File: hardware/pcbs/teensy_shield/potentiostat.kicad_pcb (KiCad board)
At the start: 2 copper layers, 144.8 x 88.9 mm, 99 parts, among them K1 CONN_3, P1 CONN_2, P10 CONN_2, P11 CONN_2, P12 CONN_2, P13 CONN_5X2, P14 CONN_5X2, P15 CONN_2X2, P16 CONN_2X2, P17 CONN_2, P18 CONN_2, P19 CONN_2, P2 CONN_2, P20 CONN_2, P21 CONN_2, P3 CONN_2, P4 CONN_2, P5 CONN_2, P6 CONN_2, P7 CONN_2, P8 CONN_2, P9 CONN_2, U1 ZXRE060, U10 OPA227, U11 OP07, U12 LT1995, U13 ADG44X, U2 TEENSY3.1, U3 MAX6176AASA+, U4 LT1995, U5 AD8250, U6 MEA1D05XXSC, U7 OPA129, U8 OPA129, U9 ADG44X

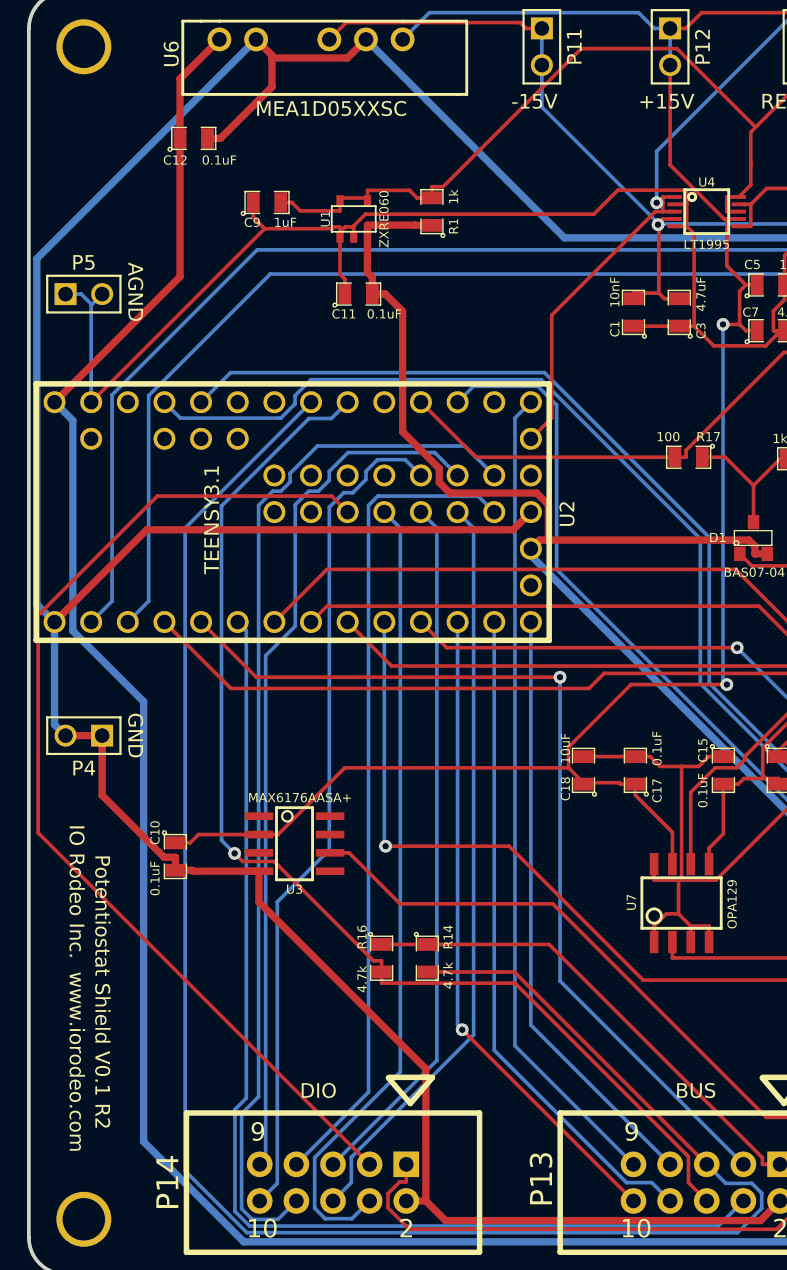
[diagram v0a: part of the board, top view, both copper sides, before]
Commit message: Modified teensy footprint - added missing hole for pin between pins 50 and 51. Modified silkscreen changed +/-15V to +/-12V.
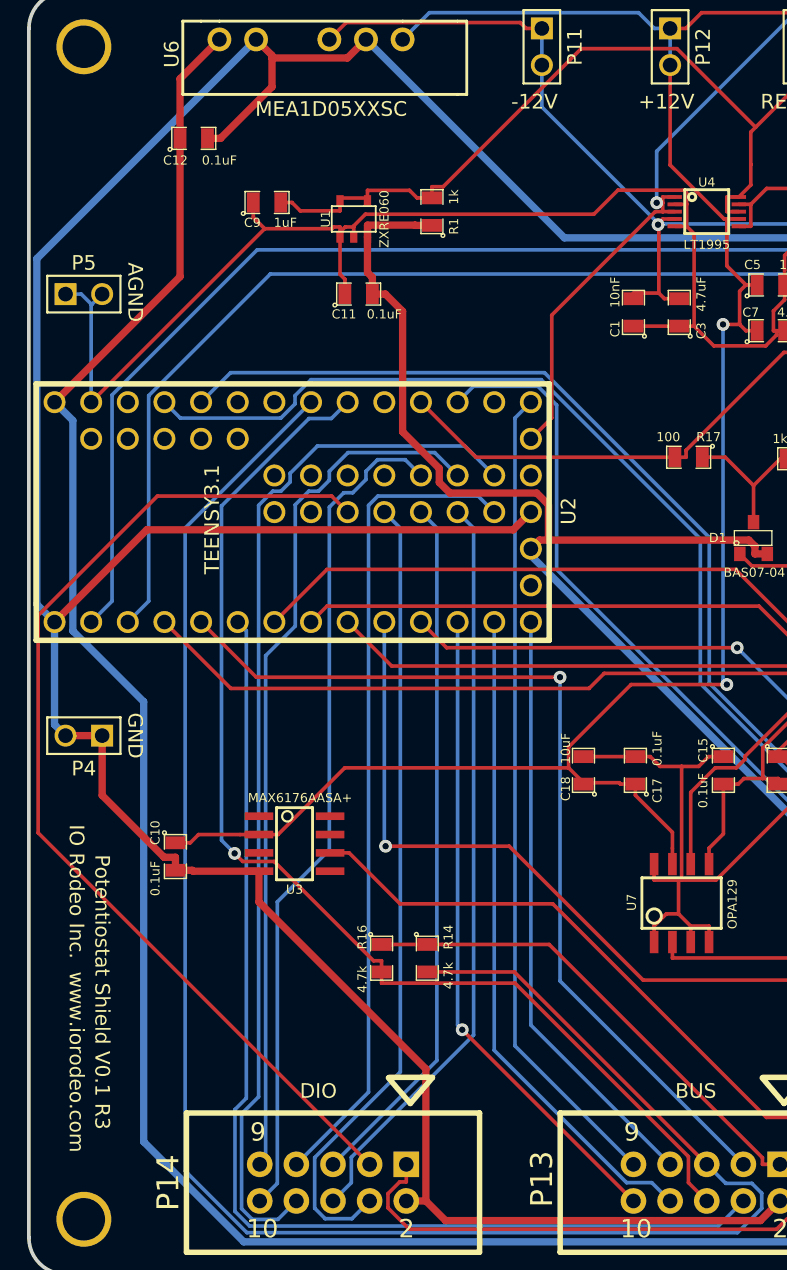
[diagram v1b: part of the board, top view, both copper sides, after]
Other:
- board text added: "+12V"
- board text added: "-12V"
- board text added: "Potentiostat Shield V0.1 R3"
- board text removed: "+15V"
- board text removed: "-15V"
- board text removed: "Potentiostat Shield V0.1 R2"
